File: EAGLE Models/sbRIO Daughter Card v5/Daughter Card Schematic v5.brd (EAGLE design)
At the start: 101.6 x 81.3 mm, 70 parts, among them IC1 BTS716G, IC2 BTS716G, IC3 BTS716G, Q7 MMBT4403-7-F, Q8 MMBT4403-7-F, U2 ADXL345, U3 L3G4200D, X1 5566-2

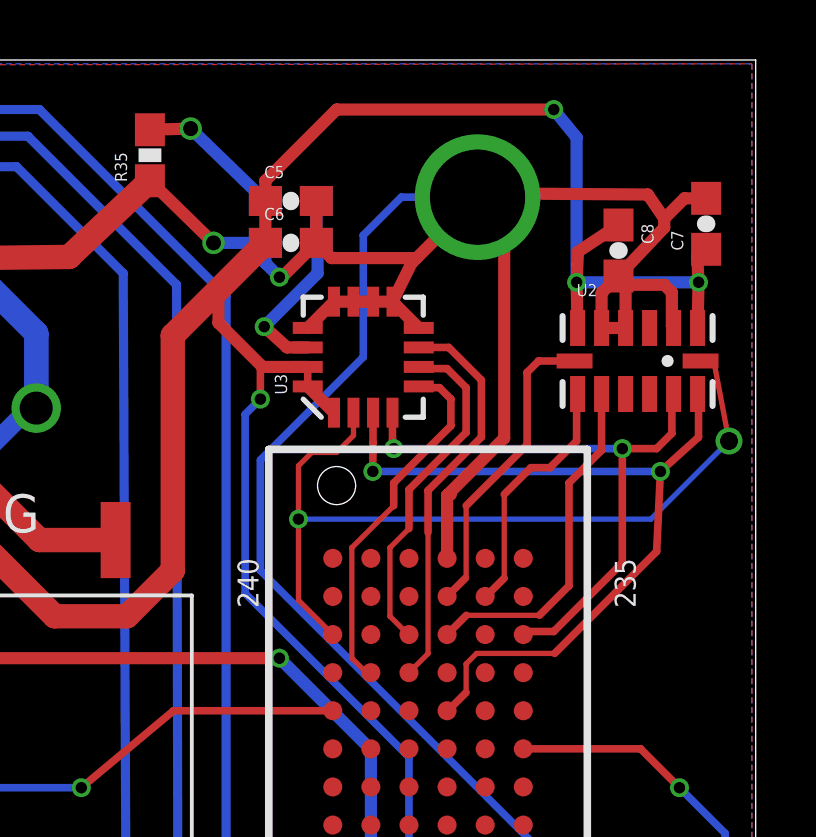
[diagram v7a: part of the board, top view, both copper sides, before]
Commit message: Extended QFN leads
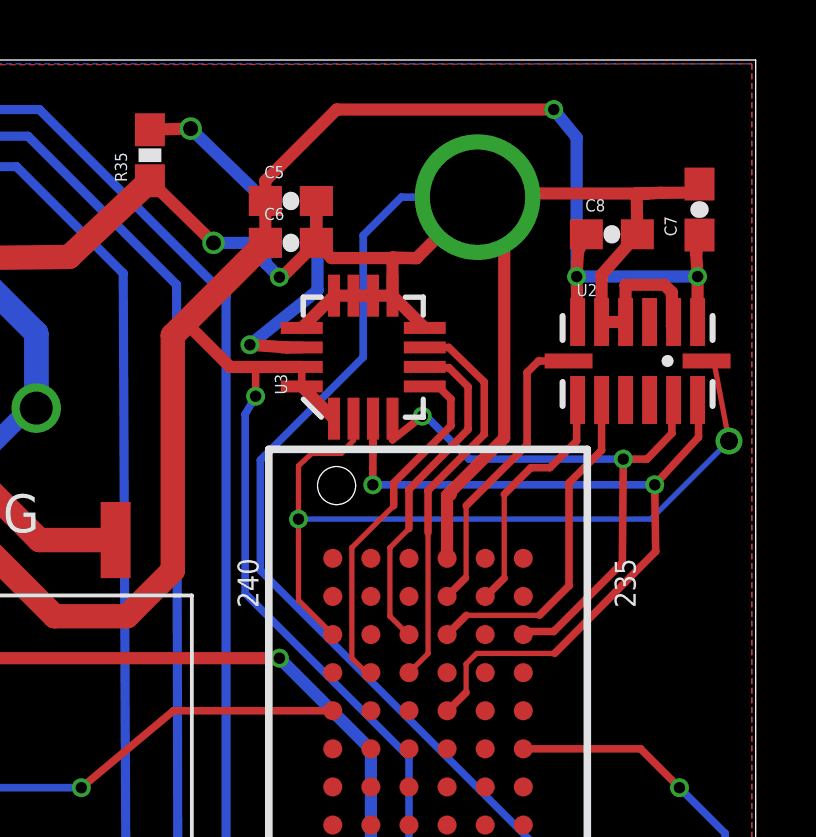
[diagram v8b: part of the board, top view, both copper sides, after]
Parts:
- moved C8 0.58 mm to (96.8, 75.5), turned to 0 degrees
- moved C7 0.53 mm to (99.7, 76.3)
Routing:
- net GND: track 703.8 -> 704.9 mm
- net 3.3V: track 97.3 -> 98.3 mm
- net N$37: track 6.66 -> 7.62 mm
